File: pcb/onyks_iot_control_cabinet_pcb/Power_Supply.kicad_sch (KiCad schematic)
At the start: 11 parts, among them J1 Screw_Terminal_01x02, J3 Jack-DC, J4 Conn_01x03_Pin, U2 LMR51430XDDCR

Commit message: PCB Overhaul
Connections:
- net +12V: now reaches C4.1, C5.1, J4.2 (Pin_2), U2.3 (VIN), U2.5 (EN)
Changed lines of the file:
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@@
+	)
+	(symbol
+		(lib_id "power:+12V")
+		(at 106.68 110.49 0)
+		(unit 1)
+		(exclude_from_sim no)
+		(in_bom yes)
+		(on_board yes)
+		(dnp no)
+		(fields_autoplaced yes)
+		(property "Reference" "#PWR028"
+			(at 106.68 114.3 0)
+			(effects
+				(font
+					(size 1.27 1.27)
+				)
+				(hide yes)
+			)
+		)
+		(property "Value" "+12V"
+			(at 106.68 105.41 0)
+			(effects
+				(font
+					(size 1.27 1.27)
+				)
+			)
+		)
+		(property "Footprint" ""
+			(at 106.68 110.49 0)
+			(effects
+				(font
+					(size 1.27 1.27)
+				)
+				(hide yes)
+			)
+		)
+		(property "Datasheet" ""
+			(at 106.68 110.49 0)
+			(effects
+				(font
+					(size 1.27 1.27)
+				)
+				(hide yes)
+			)
+		)
+		(property "Description" "Power symbol creates a global label with name \"+12V\""
+			(at 106.68 110.49 0)
+			(effects
+				(font
+					(size 1.27 1.27)
+				)
+				(hide yes)
+			)
+		)
+		(pin "1"
+		)
+		(instances
+			(project "onyks_iot_control_cabinet_pcb"
+				(path "/789878cb-67d5-4bc7-a42d-b3bc72d661d0/4d976a63-6b51-465b-8a87-51604fe7b516"
+					(reference "#PWR028")
+					(unit 1)
+				)
+			)
+		)
 	)
 	(symbol

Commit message: PCB Review 2.0 Update
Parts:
- added C8: 47n/10V, Capacitor_SMD:C_0805_2012Metric, symbol Device:C
- C7: value 100u/6.3V -> 47n/10V; footprint Capacitor_SMD:C_1210_3225Metric -> Capacitor_SMD:C_0805_2012Metric
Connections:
- net +3.3V: now also C8.1
- net GND: now also C8.2

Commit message: Quick fixes
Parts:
- renumbered C4 to C5, C5 to C6, C6 to C7, C7 to C8, C8 to C9, J1 to J3, J3 to J4, J4 to J5, R5 to R3, R6 to R4
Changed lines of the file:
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@@
 		(dnp no)
 		(fields_autoplaced yes)
-		(property "Reference" "C8"
+		(property "Reference" "C9"
 			(at 242.57 126.9999 0)
 			(effects
@@
 			(project "onyks_iot_control_cabinet_pcb"
 				(path "/789878cb-67d5-4bc7-a42d-b3bc72d661d0/4d976a63-6b51-465b-8a87-51604fe7b516"
-					(reference "C8")
+					(reference "C9")
 					(unit 1)
 				)
@@
 		(dnp no)
 		(fields_autoplaced yes)
-		(property "Reference" "R6"
+		(property "Reference" "R4"
 			(at 208.28 133.3499 0)
 			(effects
@@
 			(project "onyks_iot_control_cabinet_pcb"
 				(path "/789878cb-67d5-4bc7-a42d-b3bc72d661d0/4d976a63-6b51-465b-8a87-51604fe7b516"
-					(reference "R6")
+					(reference "R4")
 					(unit 1)
 				)
@@
 		(on_board yes)
 		(dnp no)
-		(property "Reference" "J1"
+		(property "Reference" "J3"
 			(at 64.77 99.822 0)
 			(effects
@@
 			(project "onyks_iot_control_cabinet_pcb"
 				(path "/789878cb-67d5-4bc7-a42d-b3bc72d661d0/4d976a63-6b51-465b-8a87-51604fe7b516"
-					(reference "J1")
+					(reference "J3")
 					(unit 1)
 				)
@@
 		(dnp no)
 		(fields_autoplaced yes)
-		(property "Reference" "#PWR014"
+		(property "Reference" "#PWR018"
 			(at 106.68 129.54 0)
 			(effects
@@
 			(project "onyks_iot_control_cabinet_pcb"
 				(path "/789878cb-67d5-4bc7-a42d-b3bc72d661d0/4d976a63-6b51-465b-8a87-51604fe7b516"
-					(reference "#PWR014")
+					(reference "#PWR018")
 					(unit 1)
 				)
@@
 		(dnp no)
 		(fields_autoplaced yes)
-		(property "Reference" "#PWR019"
+		(property "Reference" "#PWR020"
 			(at 146.05 130.81 0)
 			(effects
@@
 			(project "onyks_iot_control_cabinet_pcb"
 				(path "/789878cb-67d5-4bc7-a42d-b3bc72d661d0/4d976a63-6b51-465b-8a87-51604fe7b516"
-					(reference "#PWR019")
+					(reference "#PWR020")
 					(unit 1)
 				)
@@
 		(dnp no)
 		(fields_autoplaced yes)
-		(property "Reference" "#PWR028"
+		(property "Reference" "#PWR017"
 			(at 106.68 114.3 0)
 			(effects
@@
 			(project "onyks_iot_control_cabinet_pcb"
 				(path "/789878cb-67d5-4bc7-a42d-b3bc72d661d0/4d976a63-6b51-465b-8a87-51604fe7b516"
-					(reference "#PWR028")
+					(reference "#PWR017")
 					(unit 1)
 				)
@@
 		(dnp no)
 		(fields_autoplaced yes)
-		(property "Reference" "C7"
+		(property "Reference" "C8"
 			(at 226.06 126.9999 0)
 			(effects
@@
 			(project "onyks_iot_control_cabinet_pcb"
 				(path "/789878cb-67d5-4bc7-a42d-b3bc72d661d0/4d976a63-6b51-465b-8a87-51604fe7b516"
-					(reference "C7")
+					(reference "C8")
 					(unit 1)
 				)
@@
 		(dnp no)
 		(fields_autoplaced yes)
-		(property "Reference" "C6"
+		(property "Reference" "C7"
 			(at 176.53 113.0299 0)
 			(effects
@@
 			(project "onyks_iot_control_cabinet_pcb"
 				(path "/789878cb-67d5-4bc7-a42d-b3bc72d661d0/4d976a63-6b51-465b-8a87-51604fe7b516"
-					(reference "C6")
+					(reference "C7")
 					(unit 1)
 				)
@@
 		(dnp no)
 		(fields_autoplaced yes)
-		(property "Reference" "#PWR016"
+		(property "Reference" "#PWR019"
 			(at 121.92 129.54 0)
 			(effects
@@
 			(project "onyks_iot_control_cabinet_pcb"
 				(path "/789878cb-67d5-4bc7-a42d-b3bc72d661d0/4d976a63-6b51-465b-8a87-51604fe7b516"
-					(reference "#PWR016")
+					(reference "#PWR019")
 					(unit 1)
 				)
@@
 		(dnp no)
 		(fields_autoplaced yes)
-		(property "Reference" "R5"
+		(property "Reference" "R3"
 			(at 208.28 121.9199 0)
 			(effects
@@
 			(project "onyks_iot_control_cabinet_pcb"
 				(path "/789878cb-67d5-4bc7-a42d-b3bc72d661d0/4d976a63-6b51-465b-8a87-51604fe7b516"
-					(reference "R5")
+					(reference "R3")
 					(unit 1)
 				)
@@
 		(on_board yes)
 		(dnp no)
-		(property "Reference" "J4"
+		(property "Reference" "J5"
 			(at 90.424 110.49 0)
 			(effects
@@
 			(project "onyks_iot_control_cabinet_pcb"
 				(path "/789878cb-67d5-4bc7-a42d-b3bc72d661d0/4d976a63-6b51-465b-8a87-51604fe7b516"
-					(reference "J4")
+					(reference "J5")
 					(unit 1)
 				)
@@
 		(dnp no)
 		(fields_autoplaced yes)
-		(property "Reference" "C5"
+		(property "Reference" "C6"
 			(at 125.73 115.5699 0)
 			(effects
@@
 			(project "onyks_iot_control_cabinet_pcb"
 				(path "/789878cb-67d5-4bc7-a42d-b3bc72d661d0/4d976a63-6b51-465b-8a87-51604fe7b516"
-					(reference "C5")
+					(reference "C6")
 					(unit 1)
 				)
@@
 		(dnp no)
 		(fields_autoplaced yes)
-		(property "Reference" "#PWR06"
+		(property "Reference" "#PWR015"
 			(at 77.47 111.76 0)
 			(effects
@@
 			(project "onyks_iot_control_cabinet_pcb"
 				(path "/789878cb-67d5-4bc7-a42d-b3bc72d661d0/4d976a63-6b51-465b-8a87-51604fe7b516"
-					(reference "#PWR06")
+					(reference "#PWR015")
 					(unit 1)
 				)
@@
 		(dnp no)
 		(fields_autoplaced yes)
-		(property "Reference" "C4"
+		(property "Reference" "C5"
 			(at 110.49 114.2999 0)
 			(effects
@@
 			(project "onyks_iot_control_cabinet_pcb"
 				(path "/789878cb-67d5-4bc7-a42d-b3bc72d661d0/4d976a63-6b51-465b-8a87-51604fe7b516"
-					(reference "C4")
+					(reference "C5")
 					(unit 1)
 				)
@@
 		(on_board yes)
 		(dnp no)
-		(property "Reference" "J3"
+		(property "Reference" "J4"
 			(at 64.77 115.062 0)
 			(effects
@@
 			(project "onyks_iot_control_cabinet_pcb"
 				(path "/789878cb-67d5-4bc7-a42d-b3bc72d661d0/4d976a63-6b51-465b-8a87-51604fe7b516"
-					(reference "J3")
+					(reference "J4")
 					(unit 1)
 				)
@@
 		(dnp no)
 		(fields_autoplaced yes)
-		(property "Reference" "#PWR023"
+		(property "Reference" "#PWR024"
 			(at 250.19 121.92 0)
 			(effects
@@
 			(project "onyks_iot_control_cabinet_pcb"
 				(path "/789878cb-67d5-4bc7-a42d-b3bc72d661d0/4d976a63-6b51-465b-8a87-51604fe7b516"
-					(reference "#PWR023")
+					(reference "#PWR024")
 					(unit 1)
 				)
@@
 		(dnp no)
 		(fields_autoplaced yes)
-		(property "Reference" "#PWR07"
+		(property "Reference" "#PWR016"
 			(at 80.01 130.81 0)
 			(effects
@@
 			(project "onyks_iot_control_cabinet_pcb"
 				(path "/789878cb-67d5-4bc7-a42d-b3bc72d661d0/4d976a63-6b51-465b-8a87-51604fe7b516"
-					(reference "#PWR07")
+					(reference "#PWR016")
 					(unit 1)
 				)
@@
 		(dnp no)
 		(fields_autoplaced yes)
-		(property "Reference" "#PWR029"
+		(property "Reference" "#PWR023"
 			(at 238.76 149.86 0)
 			(effects
@@
 			(project "onyks_iot_control_cabinet_pcb"
 				(path "/789878cb-67d5-4bc7-a42d-b3bc72d661d0/4d976a63-6b51-465b-8a87-51604fe7b516"
-					(reference "#PWR029")
-					(unit 1)
-				)
+					(reference "#PWR023")
+					(unit 1)
+				)

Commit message: Update of the power supply; change of the stepdown from 3.3V to 5V on the output without updating the PCB
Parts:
- added C11, C12: 10u/10V, symbol Device:C_Polarized
- added U3: LM1117MP-3.3, Package_TO_SOT_SMD:SOT-223-3_TabPin2, symbol Regulator_Linear:LM1117MP-3.3
- L1: value XAL6060-562MEC_COC -> XAL6060-682MEC
- R4: value 22.1k -> 13.7k
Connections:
- net +3.3V: now also C12.1, U3.2 (VO); no longer C8.1, C9.1, L1.2, R3.1
- net GND: now also C11.2, C12.2, U3.1 (GND)
- new net +5V: C11.1, C8.1, C9.1, L1.2, R3.1, U3.3 (VI)
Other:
- note added: "5V to 3.3V"
- note added: "Stepdown to 5V"

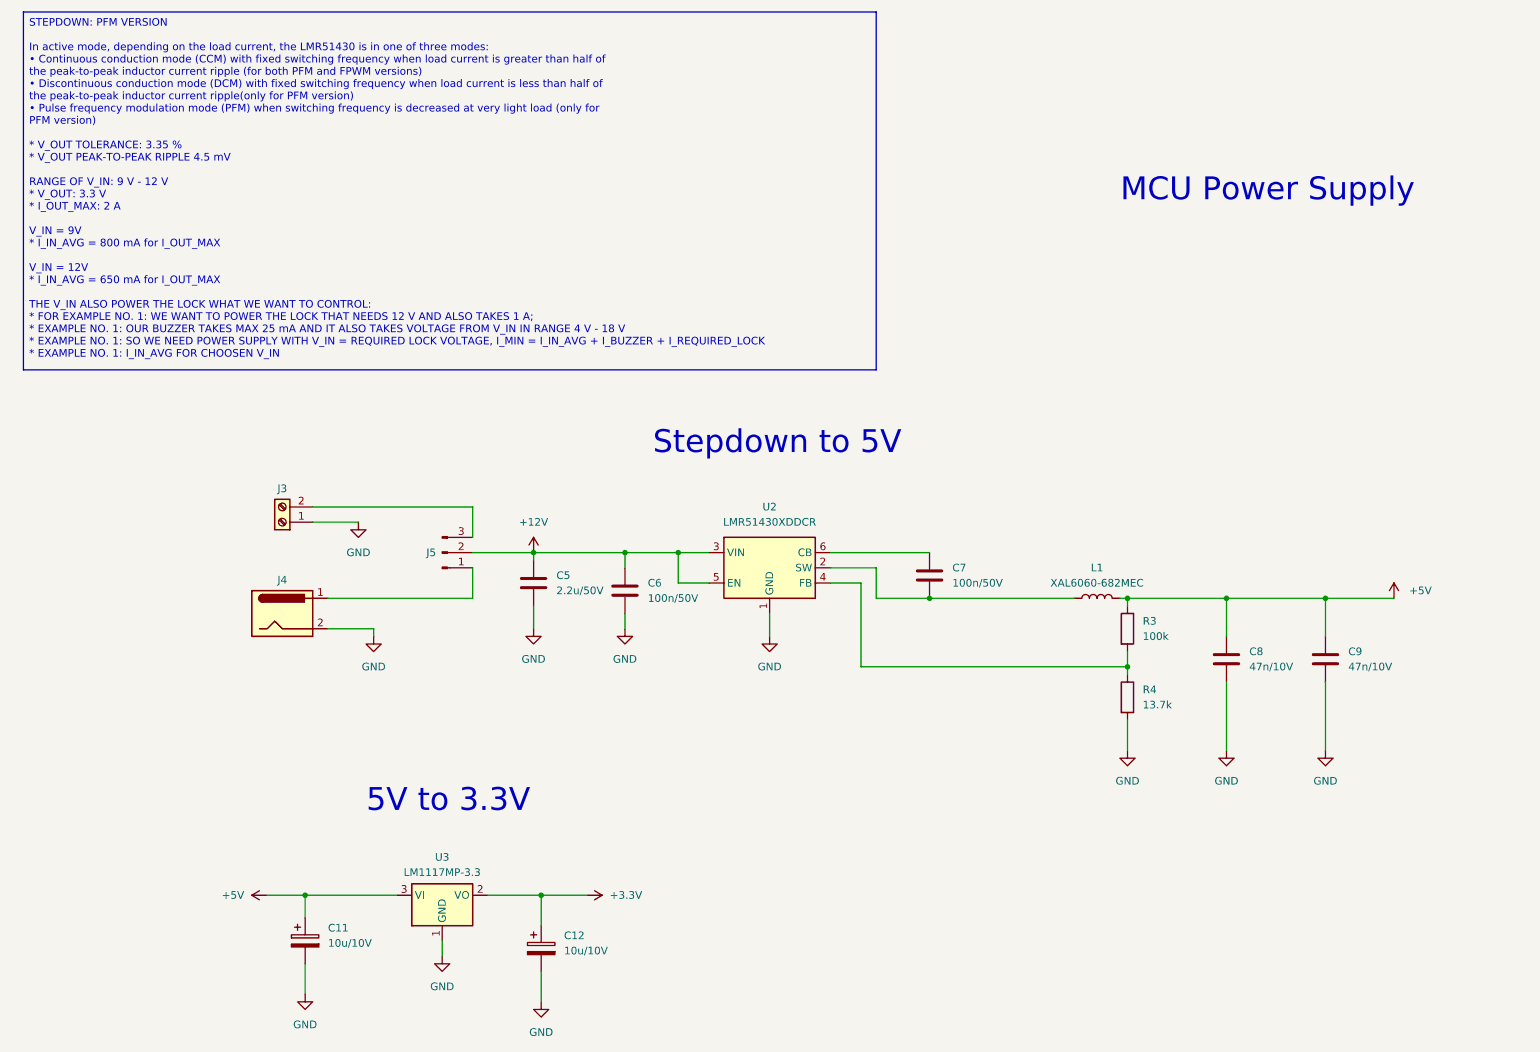
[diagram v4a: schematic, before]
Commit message: Update of the power supply and added the header for 125kHz RFID
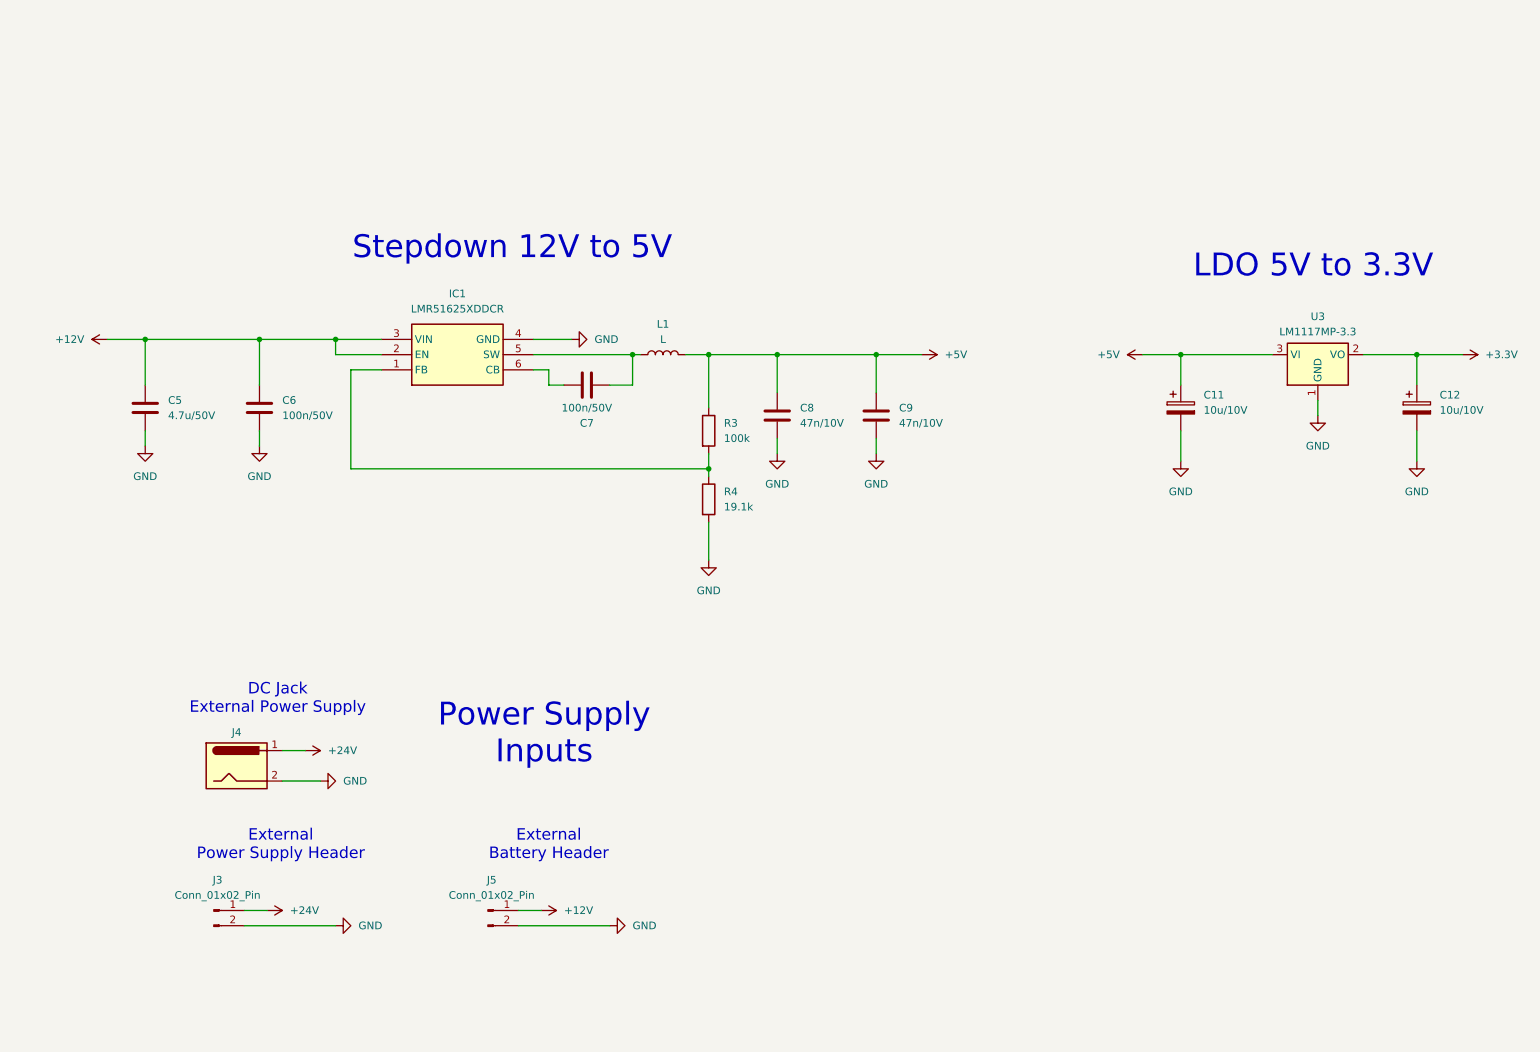
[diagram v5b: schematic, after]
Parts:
- removed J3: Screw_Terminal_01x02, TerminalBlock:TerminalBlock_Xinya_XY308-2.54-2P_1x02_P2.54mm_Horizontal, symbol Connector:Screw_Terminal_01x02
- removed J5: Conn_01x03_Pin, Connector_PinHeader_2.54mm:PinHeader_1x03_P2.54mm_Vertical, symbol Connector:Conn_01x03_Pin
- removed U2: LMR51430XDDCR, Package_TO_SOT_SMD:SOT-23-6, symbol Regulator_Switching:LMR51430
- added IC1: LMR51625XDDCR, SOT95P280X110-6N, symbol LMR51625XDDCR:LMR51625XDDCR
- added J3, J5: Conn_01x02_Pin, symbol Connector:Conn_01x02_Pin
- C5: value 2.2u/50V -> 4.7u/50V
- L1: value XAL6060-682MEC -> L; footprint ourFootprints:XAL6060-562MEC_COC -> (none)
- R4: value 13.7k -> 19.1k
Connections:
- net +12V: now also IC1.2 (EN), IC1.3 (VIN), J5.1 (Pin_1)
- net GND: now also IC1.4 (GND), J3.2 (Pin_2), J5.2 (Pin_2)
- net at R3.2, R4.1: now also IC1.1 (FB)
- net at C7.1: now also IC1.6 (CB)
- net at C7.2, L1.1: now also IC1.5 (SW)
- net +24V: now reaches J4.1
- net +24V: now also J3.1 (Pin_1)
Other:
- note added: "DC Jack External Power Supply"
- note added: "External Battery Header"
- note added: "External Power Supply Header"
- note added: "LDO 5V to 3.3V"
- note added: "Power Supply Inputs"
- note added: "Stepdown 12V to 5V"
- note removed: "5V to 3.3V"
- note removed: "MCU Power Supply"
- note removed: "Stepdown to 5V"
- company: (none) -> ,,Onyks'' Students Scientific Association
- title: (none) -> Onyks Iot Control Cabinet
- moved on the sheet: C11, C12, C5, C6, J4, U3

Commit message: Schematics update; power supply and footprints fixes
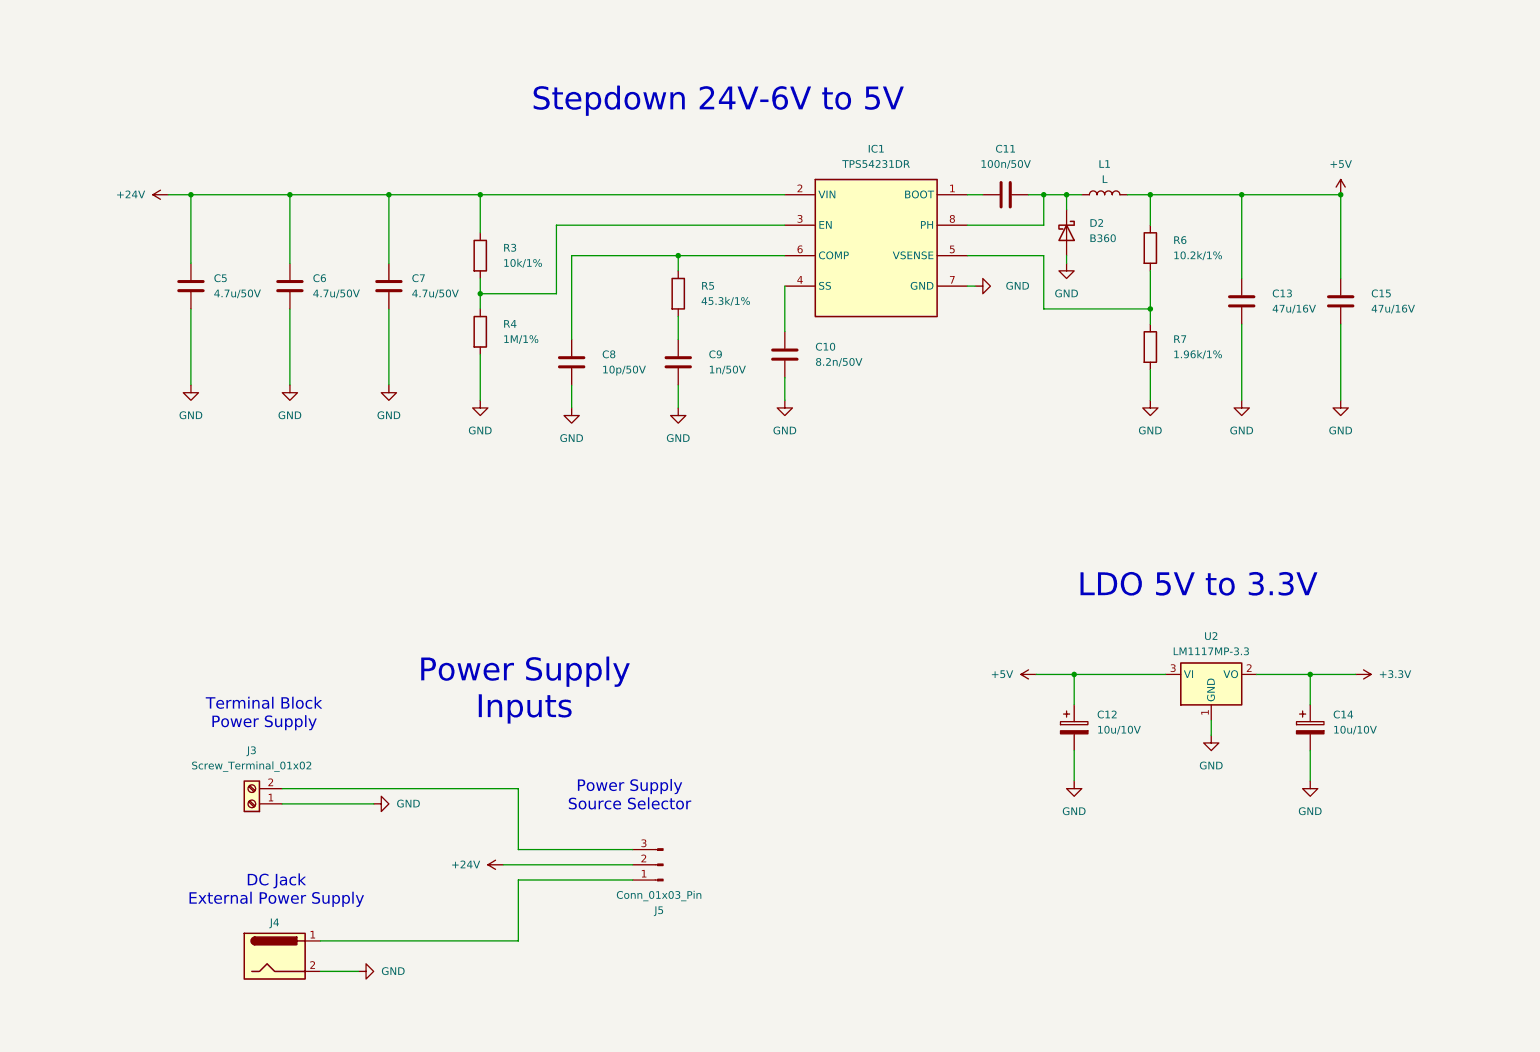
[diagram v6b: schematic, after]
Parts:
- removed IC1: LMR51625XDDCR, SOT95P280X110-6N, symbol LMR51625XDDCR:LMR51625XDDCR
- removed J3, J5: Conn_01x02_Pin, symbol Connector:Conn_01x02_Pin
- added C10: 8.2n/50V, Capacitor_SMD:C_0603_1608Metric, symbol Device:C
- added C11: 100n/50V, Capacitor_SMD:C_0603_1608Metric, symbol Device:C
- added C13, C15: 47u/16V, Capacitor_SMD:C_0603_1608Metric, symbol Device:C
- added D2: B360, Diode_SMD:D_SMC, symbol Diode:B360
- added IC1: TPS54231DR, footprints:SOIC127P600X175-8N, symbol TPS54231DR:TPS54231DR
- added J3: Screw_Terminal_01x02, TerminalBlock:TerminalBlock_Altech_AK300-2_P5.00mm, symbol Connector:Screw_Terminal_01x02
- added J5: Conn_01x03_Pin, Connector_PinHeader_2.54mm:PinHeader_1x03_P2.54mm_Horizontal, symbol Connector:Conn_01x03_Pin
- added R5: 45.3k/1%, Resistor_SMD:R_0805_2012Metric_Pad1.20x1.40mm_HandSolder, symbol Device:R
- added R6: 10.2k/1%, Resistor_SMD:R_0805_2012Metric_Pad1.20x1.40mm_HandSolder, symbol Device:R
- added R7: 1.96k/1%, Resistor_SMD:R_0805_2012Metric_Pad1.20x1.40mm_HandSolder, symbol Device:R
- C12: renamed from C11; footprint (none) -> Capacitor_SMD:C_0603_1608Metric
- C14: renamed from C12; footprint (none) -> Capacitor_SMD:C_0603_1608Metric
- C6: value 100n/50V -> 4.7u/50V
- C7: value 100n/50V -> 4.7u/50V; footprint Capacitor_SMD:C_0805_2012Metric -> Capacitor_SMD:C_0603_1608Metric
- C8: value 47n/10V -> 10p/50V; footprint Capacitor_SMD:C_0805_2012Metric -> Capacitor_SMD:C_0603_1608Metric
- C9: value 47n/10V -> 1n/50V; footprint Capacitor_SMD:C_0805_2012Metric -> Capacitor_SMD:C_0603_1608Metric
- J4: footprint Connector_BarrelJack:BarrelJack_CUI_PJ-036AH-SMT_Horizontal -> Connector_BarrelJack:BarrelJack_CLIFF_FC681465S_SMT_Horizontal
- L1: footprint (none) -> Inductor_SMD:L_12x12mm_H4.5mm
- R3: value 100k -> 10k/1%
- R4: value 19.1k -> 1M/1%
- renumbered U3 to U2
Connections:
- net +12V is gone; now on net +24V: C5.1, C6.1
- net +24V: now also C7.1, R3.1, IC1.2 (VIN), J5.2 (Pin_2); no longer J4.1
- net +5V: now also C13.1, C15.1, R6.1; no longer C8.1, C9.1, R3.1
- net GND: now also C7.2, C10.2, C13.2, C15.2, D2.2 (A), IC1.7 (GND), J3.1 (Pin_1), R7.2
- net at R3.2, R4.1: now also IC1.3 (EN)
- net at L1.1: now also C11.2, D2.1 (K), IC1.8 (PH); no longer C7.2
- new net: J3.2 (Pin_2), J5.3 (Pin_3)
- new net: J4.1, J5.1 (Pin_1)
- new net: C10.1, IC1.4 (SS)
- new net: IC1.5 (VSENSE), R6.2, R7.1
- new net: C11.1, IC1.1 (BOOT)
- new net: C8.1, IC1.6 (COMP), R5.1
- new net: C9.1, R5.2
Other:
- note added: "Power Supply Source Selector"
- note added: "Stepdown 24V-6V to 5V"
- note added: "Terminal Block Power Supply"
- note removed: "External Battery Header"
- note removed: "External Power Supply Header"
- note removed: "Stepdown 12V to 5V"
- moved on the sheet: C12, C14, J4, U2
